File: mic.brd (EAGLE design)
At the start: 45.7 x 20.3 mm, 10 parts, among them IC1 AD8614RJ, M1 ELECTRET_MICROPHON-WM.64PN

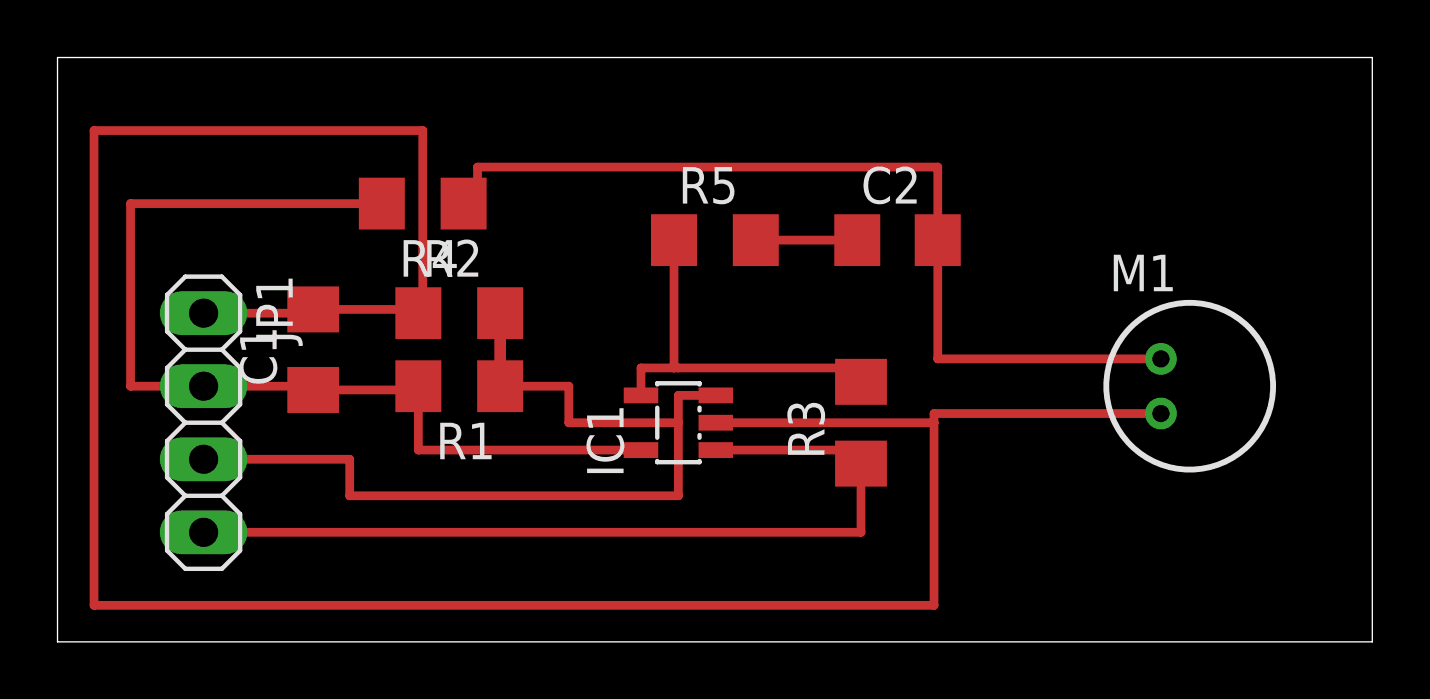
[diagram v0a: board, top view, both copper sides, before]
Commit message: Breakout board and PNGs for electret mic circuit.
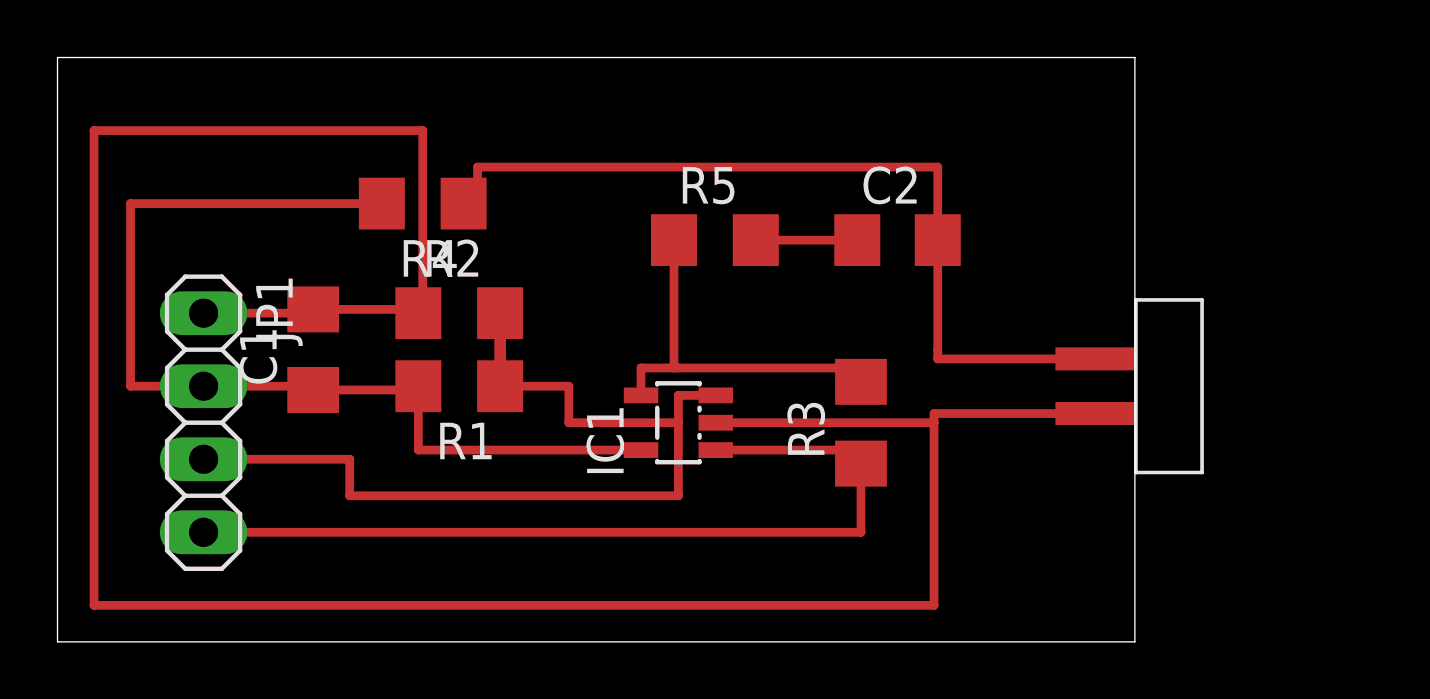
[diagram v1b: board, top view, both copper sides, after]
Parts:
- removed M1: ELECTRET_MICROPHON-WM.64PN, microphon:WM-64PN
- added U$1: ELECTRET, LED Light:ELECTRET_6MM_SMD
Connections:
- net GND: now also U$1.P$2; no longer M1.2
- net N$4: now also U$1.P$1; no longer M1.1
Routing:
- net N$4: track 32.2 -> 29.9 mm
- net GND: track 93.5 -> 91.3 mm
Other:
- board size 45.7 x 20.3 mm -> 37.5 x 20.3 mm
